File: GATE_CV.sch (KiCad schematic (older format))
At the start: 69 parts, among them J801 TRG0, J802 CVIN1, J803 CVIN3, J804 CVIN2, J805 CVIN4, J806 TRG1, J807 CVIN4, J808 CVIN4, J809 CVIN4, J810 CVIN4, Q801 Q_NPN_BEC, Q802 Q_NPN_BEC, SW801 TRG0, SW802 TRG1, U801 MCP6004, U802 MCP6004, U803 MCP3208

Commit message: current
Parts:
- removed TP801: TA, TestPoint:TestPoint_Keystone_5019_Minature, symbol Connector:TestPoint
- removed TP802: TB, TestPoint:TestPoint_Keystone_5019_Minature, symbol Connector:TestPoint
- removed TP803: TC, TestPoint:TestPoint_Keystone_5019_Minature, symbol Connector:TestPoint
- J808: value CVIN4 -> CVIN5
- J809: value CVIN4 -> CVIN6
- J810: value CVIN4 -> CVIN7
- R801, R814: value 10k -> 0
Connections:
- net at R829.2: now also J808.1; no longer J809.1
- net at R824.2: now also J809.1; no longer J808.1
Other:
- moved on the sheet: J808, J809
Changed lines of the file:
@@
 Sheet 8 8
 Title "ESP32 Eurorack Audio Module"
-Date "2019-03-27"
-Rev "B2-public"
+Date "2019-04-27"
+Rev "C2"
 Comp "(c) Robert Manzke 2019"
 Comment1 "https://creativecommons.org/licenses/by-nc-sa/4.0/"
@@
 P 3650 2100
 F 0 "R801" H 3580 2054 50  0000 R CNN
-F 1 "10k" H 3580 2145 50  0000 R CNN
+F 1 "0" H 3580 2145 50  0000 R CNN
 F 2 "Resistor_SMD:R_0603_1608Metric" V 3580 2100 50  0001 C CNN
 F 3 "~" H 3650 2100 50  0001 C CNN
@@
 P 3600 4450
 F 0 "R814" H 3530 4404 50  0000 R CNN
-F 1 "10k" H 3530 4495 50  0000 R CNN
+F 1 "0" H 3530 4495 50  0000 R CNN
 F 2 "Resistor_SMD:R_0603_1608Metric" V 3530 4450 50  0001 C CNN
 F 3 "~" H 3600 4450 50  0001 C CNN
@@
 L jack_2p:JACK_2P J809
 U 1 1 5B9A8472
-P 6500 8400
-F 0 "J809" H 6022 8384 50  0000 R CNN
-F 1 "CVIN4" H 6022 8475 50  0000 R CNN
-F 2 "connectors:THONKICONN" H 6500 8400 50  0001 C CNN
-F 3 "" H 6500 8400 50  0000 C CNN
-	1    6500 8400
+P 10300 6800
+F 0 "J809" H 9822 6784 50  0000 R CNN
+F 1 "CVIN6" H 9822 6875 50  0000 R CNN
+F 2 "connectors:THONKICONN" H 10300 6800 50  0001 C CNN
+F 3 "" H 10300 6800 50  0000 C CNN
+	1    10300 6800
 	1    0    0    1
 $EndComp
@@
 L jack_2p:JACK_2P J808
 U 1 1 5B9B27D5
-P 10300 6800
-F 0 "J808" H 9822 6784 50  0000 R CNN
-F 1 "CVIN4" H 9822 6875 50  0000 R CNN
-F 2 "connectors:THONKICONN" H 10300 6800 50  0001 C CNN
-F 3 "" H 10300 6800 50  0000 C CNN
-	1    10300 6800
+P 6500 8400
+F 0 "J808" H 6022 8384 50  0000 R CNN
+F 1 "CVIN5" H 6022 8475 50  0000 R CNN
+F 2 "connectors:THONKICONN" H 6500 8400 50  0001 C CNN
+F 3 "" H 6500 8400 50  0000 C CNN
+	1    6500 8400
 	1    0    0    1
 $EndComp
@@
 P 10300 8400
 F 0 "J810" H 9822 8384 50  0000 R CNN
-F 1 "CVIN4" H 9822 8475 50  0000 R CNN
+F 1 "CVIN7" H 9822 8475 50  0000 R CNN
 F 2 "connectors:THONKICONN" H 10300 8400 50  0001 C CNN
 F 3 "" H 10300 8400 50  0000 C CNN
@@
 Text Label 1950 8250 0    50   ~ 0
 CVIN7
-Wire Wire Line
-	3600 7750 3750 7750
-Wire Wire Line
-	3600 7950 4050 7950
-Wire Wire Line
-	3600 8050 4200 8050
 Text HLabel 4300 7750 2    50   Input ~ 0
 MCP_CLK
@@
 Wire Wire Line
 	1750 9250 1750 9300
-$Comp
-L Connector:TestPoint TP801
-U 1 1 5BDED682
-P 3750 7650
-F 0 "TP801" H 3700 8000 50  0000 L CNN
-F 1 "TA" H 3700 7900 50  0000 L CNN
-F 2 "TestPoint:TestPoint_Keystone_5019_Minature" H 3950 7650 50  0001 C CNN
-F 3 "~" H 3950 7650 50  0001 C CNN
-	1    3750 7650
-	1    0    0    -1
-$EndComp
-$Comp
-L Connector:TestPoint TP802
-U 1 1 5BE10843
-P 4050 7650
-F 0 "TP802" V 3950 7650 50  0000 L CNN
-F 1 "TB" H 4000 7900 50  0000 L CNN
-F 2 "TestPoint:TestPoint_Keystone_5019_Minature" H 4250 7650 50  0001 C CNN
-F 3 "~" H 4250 7650 50  0001 C CNN
-	1    4050 7650
-	1    0    0    -1
-$EndComp
-$Comp
-L Connector:TestPoint TP803
-U 1 1 5BE108EF
-P 4200 7650
-F 0 "TP803" H 4150 8000 50  0000 L CNN
-F 1 "TC" H 4150 7900 50  0000 L CNN
-F 2 "TestPoint:TestPoint_Keystone_5019_Minature" H 4400 7650 50  0001 C CNN
-F 3 "~" H 4400 7650 50  0001 C CNN
-	1    4200 7650
-	1    0    0    -1
-$EndComp
-Wire Wire Line
-	3750 7650 3750 7750
-Connection ~ 3750 7750
-Wire Wire Line
-	3750 7750 4300 7750
-Wire Wire Line
-	4050 7650 4050 7950
-Connection ~ 4050 7950
-Wire Wire Line
-	4050 7950 4300 7950
-Wire Wire Line
-	4200 7650 4200 8050
-Connection ~ 4200 8050
-Wire Wire Line
-	4200 8050 4300 8050
 Wire Wire Line
 	3600 7850 4300 7850
@@
 Text Notes 6100 9550 0    50   ~ 0
 This section is pretty much taken from \nMutable Instruments Clouds (c) Olivier Gillet
+Wire Wire Line
+	3600 8050 4300 8050
+Wire Wire Line
+	3600 7950 4300 7950
+Wire Wire Line
+	3600 7750 4300 7750
 $EndSCHEMATC

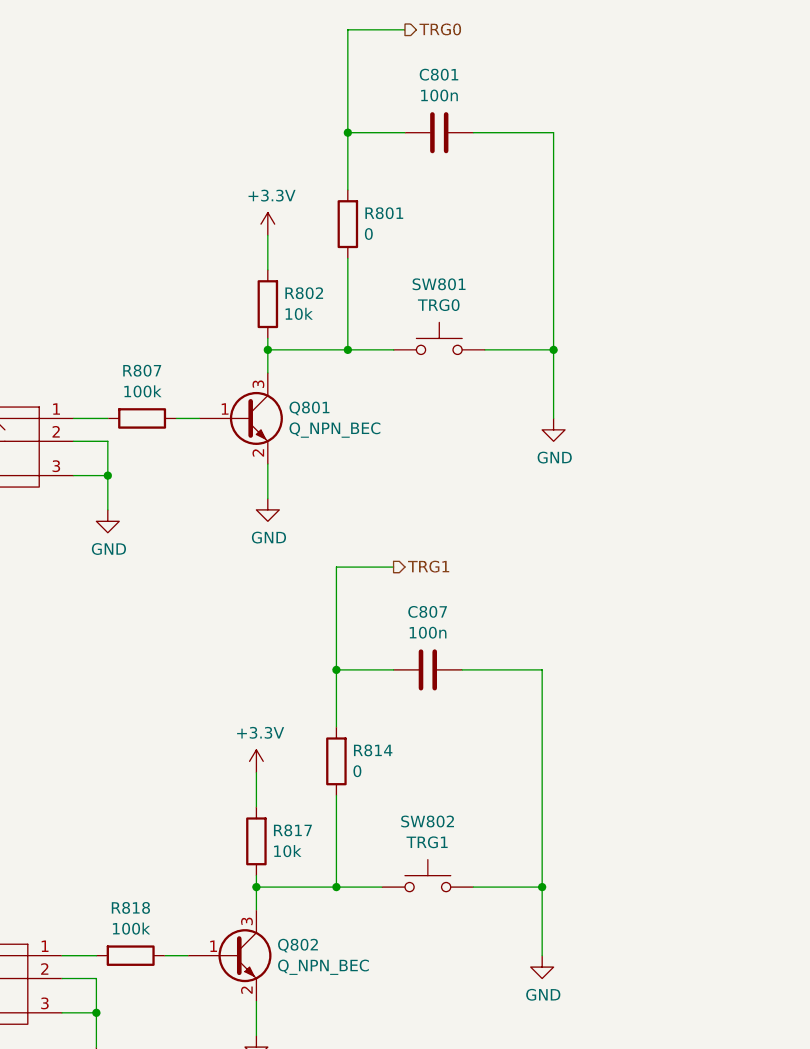
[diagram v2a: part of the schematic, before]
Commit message: cleaned up schematic
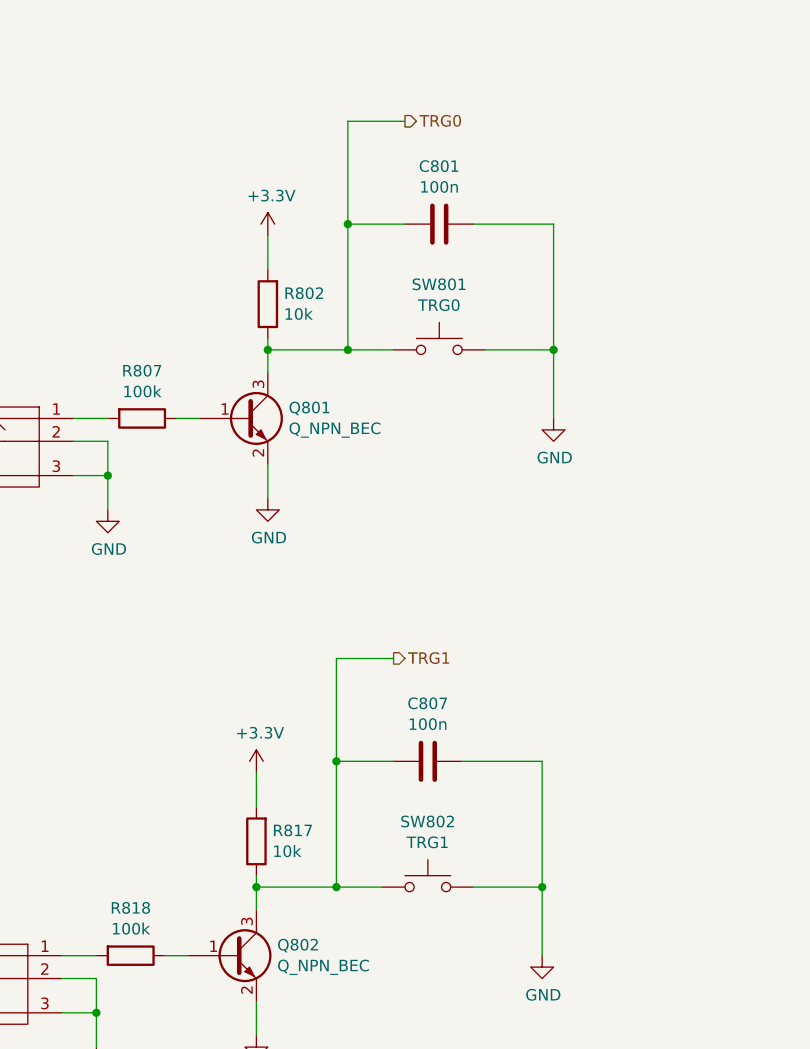
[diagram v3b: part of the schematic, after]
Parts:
- removed R801, R814: 0, Resistor_SMD:R_0603_1608Metric, symbol Device:R
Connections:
- net TRG0: now also Q801.3 (C), R802.1, SW801.1
- net TRG1: now also Q802.3 (C), R817.1, SW802.1
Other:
- moved on the sheet: C801, C807
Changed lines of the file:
@@
 Sheet 8 8
 Title "ESP32 Eurorack Audio Module"
-Date "2019-04-27"
-Rev "C2"
+Date "2019-05-13"
+Rev "D"
 Comp "(c) Robert Manzke 2019"
 Comment1 "https://creativecommons.org/licenses/by-nc-sa/4.0/"
@@
 	2600 3050 2600 3200
 Connection ~ 2600 3200
-Wire Wire Line
-	3850 2650 3650 2650
 Connection ~ 3300 2650
 Wire Wire Line
 	3300 2650 3300 2750
-Connection ~ 3650 2650
-Wire Wire Line
-	3650 2650 3300 2650
 $Comp
 L power:GND #PWR0804
@@
 	4550 2650 4550 2950
 $Comp
-L Device:R R801
-U 1 1 5B6BF14F
-P 3650 2100
-F 0 "R801" H 3580 2054 50  0000 R CNN
-F 1 "0" H 3580 2145 50  0000 R CNN
-F 2 "Resistor_SMD:R_0603_1608Metric" V 3580 2100 50  0001 C CNN
-F 3 "~" H 3650 2100 50  0001 C CNN
-	1    3650 2100
-	-1   0    0    1
-$EndComp
-$Comp
 L Device:C C801
 U 1 1 5B6BF2F0
-P 4050 1700
-F 0 "C801" V 3798 1700 50  0000 C CNN
-F 1 "100n" V 3889 1700 50  0000 C CNN
-F 2 "Capacitor_SMD:C_0603_1608Metric" H 4088 1550 50  0001 C CNN
-F 3 "~" H 4050 1700 50  0001 C CNN
-	1    4050 1700
-	0    1    1    0
-$EndComp
-Wire Wire Line
-	3900 1700 3650 1700
-Wire Wire Line
-	3650 1700 3650 1950
-Wire Wire Line
-	4200 1700 4550 1700
-Text HLabel 3900 1250 2    50   Output ~ 0
+P 4050 2100
+F 0 "C801" V 3798 2100 50  0000 C CNN
+F 1 "100n" V 3889 2100 50  0000 C CNN
+F 2 "Capacitor_SMD:C_0603_1608Metric" H 4088 1950 50  0001 C CNN
+F 3 "~" H 4050 2100 50  0001 C CNN
+	1    4050 2100
+	0    1    1    0
+$EndComp
+Wire Wire Line
+	3900 2100 3650 2100
+Wire Wire Line
+	4200 2100 4550 2100
+Text HLabel 3900 1650 2    50   Output ~ 0
 TRG0
 Wire Wire Line
-	3900 1250 3650 1250
-Wire Wire Line
-	3650 1250 3650 1700
-Connection ~ 3650 1700
+	3900 1650 3650 1650
+Wire Wire Line
+	3650 1650 3650 2100
 $Comp
 L jack_2p:JACK_2P J806
@@
 	2550 5400 2550 5550
 Connection ~ 2550 5550
-Wire Wire Line
-	3800 5000 3600 5000
 Connection ~ 3250 5000
 Wire Wire Line
 	3250 5000 3250 5100
-Connection ~ 3600 5000
-Wire Wire Line
-	3600 5000 3250 5000
 $Comp
 L power:GND #PWR0820
@@
 	4500 5000 4500 5300
 $Comp
-L Device:R R814
-U 1 1 5B6C0356
-P 3600 4450
-F 0 "R814" H 3530 4404 50  0000 R CNN
-F 1 "0" H 3530 4495 50  0000 R CNN
-F 2 "Resistor_SMD:R_0603_1608Metric" V 3530 4450 50  0001 C CNN
-F 3 "~" H 3600 4450 50  0001 C CNN
-	1    3600 4450
-	-1   0    0    1
-$EndComp
-$Comp
 L Device:C C807
 U 1 1 5B6C035E
-P 4000 4050
-F 0 "C807" V 3748 4050 50  0000 C CNN
-F 1 "100n" V 3839 4050 50  0000 C CNN
-F 2 "Capacitor_SMD:C_0603_1608Metric" H 4038 3900 50  0001 C CNN
-F 3 "~" H 4000 4050 50  0001 C CNN
-	1    4000 4050
-	0    1    1    0
-$EndComp
-Wire Wire Line
-	3850 4050 3600 4050
-Wire Wire Line
-	3600 4050 3600 4300
-Wire Wire Line
-	4150 4050 4500 4050
-Text HLabel 3850 3600 2    50   Output ~ 0
+P 4000 4450
+F 0 "C807" V 3748 4450 50  0000 C CNN
+F 1 "100n" V 3839 4450 50  0000 C CNN
+F 2 "Capacitor_SMD:C_0603_1608Metric" H 4038 4300 50  0001 C CNN
+F 3 "~" H 4000 4450 50  0001 C CNN
+	1    4000 4450
+	0    1    1    0
+$EndComp
+Wire Wire Line
+	3850 4450 3600 4450
+Wire Wire Line
+	4150 4450 4500 4450
+Text HLabel 3850 4000 2    50   Output ~ 0
 TRG1
 Wire Wire Line
-	3850 3600 3600 3600
-Wire Wire Line
-	3600 3600 3600 4050
-Connection ~ 3600 4050
+	3850 4000 3600 4000
+Wire Wire Line
+	3600 4000 3600 4450
 $Comp
 L Switch:SW_Push SW801
@@
 $EndComp
 Wire Wire Line
-	4500 4050 4500 5000
-Wire Wire Line
-	3600 4600 3600 5000
-Wire Wire Line
-	3650 2250 3650 2650
-Wire Wire Line
-	4550 1700 4550 2650
+	4500 4450 4500 5000
+Wire Wire Line
+	4550 2100 4550 2650
 $Comp
 L Amplifier_Operational:MCP6004 U801
@@
 Wire Wire Line
 	3600 7750 4300 7750
+Wire Wire Line
+	3300 2650 3650 2650
+Wire Wire Line
+	3650 2100 3650 2650
+Connection ~ 3650 2100
+Connection ~ 3650 2650
+Wire Wire Line
+	3650 2650 3850 2650
+Wire Wire Line
+	3250 5000 3600 5000
+Wire Wire Line
+	3600 4450 3600 5000
+Connection ~ 3600 4450
+Connection ~ 3600 5000
+Wire Wire Line
+	3600 5000 3800 5000
 $EndSCHEMATC
